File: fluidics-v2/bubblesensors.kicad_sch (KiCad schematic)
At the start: 6 parts, among them U8 TC7PZ17FU, U9 CD4050BDR

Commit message: started layout
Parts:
- renumbered C3 to C?, C4 to C?, U9 to U10, U8 to U11
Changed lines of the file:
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@@
   (symbol (lib_id "TC7PZ17FU:TC7PZ17FU") (at 41.91 22.86 0) (unit 1)
     (in_bom yes) (on_board yes) (dnp no)
-    (property "Reference" "U8" (at 40.64 20.32 0)
+    (property "Reference" "U11" (at 40.64 20.32 0)
       (effects (font (size 1.524 1.524)))
     )
@@
       (project "fluidics-v2"
         (path "/0ec91c42-8aad-437d-8c85-5e10f0e51fe0/f2389ff6-1cd8-47ea-9589-49f16bb8c559"
-          (reference "U8") (unit 1)
+          (reference "U11") (unit 1)
         )
       )
@@
   (symbol (lib_id "power:+3.3V") (at 29.21 64.77 0) (unit 1)
     (in_bom yes) (on_board yes) (dnp no)
-    (property "Reference" "#PWR061" (at 29.21 68.58 0)
+    (property "Reference" "#PWR?" (at 29.21 68.58 0)
       (effects (font (size 1.27 1.27)) hide)
     )
@@
       (project "fluidics-v2"
         (path "/0ec91c42-8aad-437d-8c85-5e10f0e51fe0/978ef52c-7a59-4000-92fc-4e58ca2b1aa7"
-          (reference "#PWR0131") (unit 1)
-        )
-        (path "/0ec91c42-8aad-437d-8c85-5e10f0e51fe0/f2389ff6-1cd8-47ea-9589-49f16bb8c559"
-          (reference "#PWR0128") (unit 1)
+          (reference "#PWR?") (unit 1)
+        )
+        (path "/0ec91c42-8aad-437d-8c85-5e10f0e51fe0/f2389ff6-1cd8-47ea-9589-49f16bb8c559"
+          (reference "#PWR0124") (unit 1)
         )
       )
@@
   (symbol (lib_id "Device:C") (at 29.21 68.58 0) (unit 1)
     (in_bom yes) (on_board yes) (dnp no)
-    (property "Reference" "C3" (at 25.4 71.12 0)
+    (property "Reference" "C?" (at 25.4 71.12 0)
       (effects (font (size 1.27 1.27)) (justify left))
     )
@@
       (project "fluidics-v2"
         (path "/0ec91c42-8aad-437d-8c85-5e10f0e51fe0/c1c30de3-a3db-48df-8d6b-b2f91b9251f0"
-          (reference "C3") (unit 1)
-        )
-        (path "/0ec91c42-8aad-437d-8c85-5e10f0e51fe0/978ef52c-7a59-4000-92fc-4e58ca2b1aa7"
-          (reference "C38") (unit 1)
-        )
-        (path "/0ec91c42-8aad-437d-8c85-5e10f0e51fe0/f2389ff6-1cd8-47ea-9589-49f16bb8c559"
-          (reference "C36") (unit 1)
+          (reference "C?") (unit 1)
+        )
+        (path "/0ec91c42-8aad-437d-8c85-5e10f0e51fe0/978ef52c-7a59-4000-92fc-4e58ca2b1aa7"
+          (reference "C?") (unit 1)
+        )
+        (path "/0ec91c42-8aad-437d-8c85-5e10f0e51fe0/f2389ff6-1cd8-47ea-9589-49f16bb8c559"
+          (reference "C21") (unit 1)
         )
       )
@@
   (symbol (lib_id "power:GND") (at 40.64 93.98 0) (unit 1)
     (in_bom yes) (on_board yes) (dnp no) (fields_autoplaced)
-    (property "Reference" "#PWR0131" (at 40.64 100.33 0)
+    (property "Reference" "#PWR0128" (at 40.64 100.33 0)
       (effects (font (size 1.27 1.27)) hide)
     )
@@
       (project "fluidics-v2"
         (path "/0ec91c42-8aad-437d-8c85-5e10f0e51fe0/f2389ff6-1cd8-47ea-9589-49f16bb8c559"
-          (reference "#PWR0131") (unit 1)
+          (reference "#PWR0128") (unit 1)
         )
       )
@@
   (symbol (lib_id "Device:C") (at 25.4 44.45 0) (unit 1)
     (in_bom yes) (on_board yes) (dnp no)
-    (property "Reference" "C4" (at 21.59 46.99 0)
+    (property "Reference" "C?" (at 21.59 46.99 0)
       (effects (font (size 1.27 1.27)) (justify left))
     )
@@
       (project "fluidics-v2"
         (path "/0ec91c42-8aad-437d-8c85-5e10f0e51fe0/c1c30de3-a3db-48df-8d6b-b2f91b9251f0"
-          (reference "C4") (unit 1)
-        )
-        (path "/0ec91c42-8aad-437d-8c85-5e10f0e51fe0/978ef52c-7a59-4000-92fc-4e58ca2b1aa7"
-          (reference "C37") (unit 1)
-        )
-        (path "/0ec91c42-8aad-437d-8c85-5e10f0e51fe0/f2389ff6-1cd8-47ea-9589-49f16bb8c559"
-          (reference "C33") (unit 1)
+          (reference "C?") (unit 1)
+        )
+        (path "/0ec91c42-8aad-437d-8c85-5e10f0e51fe0/978ef52c-7a59-4000-92fc-4e58ca2b1aa7"
+          (reference "C?") (unit 1)
+        )
+        (path "/0ec91c42-8aad-437d-8c85-5e10f0e51fe0/f2389ff6-1cd8-47ea-9589-49f16bb8c559"
+          (reference "C20") (unit 1)
         )
       )
@@
   (symbol (lib_id "power:GND") (at 35.56 48.26 0) (unit 1)
     (in_bom yes) (on_board yes) (dnp no)
-    (property "Reference" "#PWR0124" (at 35.56 54.61 0)
+    (property "Reference" "#PWR?" (at 35.56 54.61 0)
       (effects (font (size 1.27 1.27)) hide)
     )
@@
       (project "fluidics-v2"
         (path "/0ec91c42-8aad-437d-8c85-5e10f0e51fe0/978ef52c-7a59-4000-92fc-4e58ca2b1aa7"
-          (reference "#PWR0132") (unit 1)
+          (reference "#PWR?") (unit 1)
         )
         (path "/0ec91c42-8aad-437d-8c85-5e10f0e51fe0/f2389ff6-1cd8-47ea-9589-49f16bb8c559"
@@
   (symbol (lib_id "Device:C") (at 35.56 44.45 0) (unit 1)
     (in_bom yes) (on_board yes) (dnp no)
-    (property "Reference" "C3" (at 31.75 46.99 0)
+    (property "Reference" "C?" (at 31.75 46.99 0)
       (effects (font (size 1.27 1.27)) (justify left))
     )
@@
       (project "fluidics-v2"
         (path "/0ec91c42-8aad-437d-8c85-5e10f0e51fe0/c1c30de3-a3db-48df-8d6b-b2f91b9251f0"
-          (reference "C3") (unit 1)
-        )
-        (path "/0ec91c42-8aad-437d-8c85-5e10f0e51fe0/978ef52c-7a59-4000-92fc-4e58ca2b1aa7"
-          (reference "C38") (unit 1)
-        )
-        (path "/0ec91c42-8aad-437d-8c85-5e10f0e51fe0/f2389ff6-1cd8-47ea-9589-49f16bb8c559"
-          (reference "C34") (unit 1)
+          (reference "C?") (unit 1)
+        )
+        (path "/0ec91c42-8aad-437d-8c85-5e10f0e51fe0/978ef52c-7a59-4000-92fc-4e58ca2b1aa7"
+          (reference "C?") (unit 1)
+        )
+        (path "/0ec91c42-8aad-437d-8c85-5e10f0e51fe0/f2389ff6-1cd8-47ea-9589-49f16bb8c559"
+          (reference "C22") (unit 1)
         )
       )
@@
   (symbol (lib_id "Device:C") (at 19.05 68.58 0) (unit 1)
     (in_bom yes) (on_board yes) (dnp no)
-    (property "Reference" "C4" (at 15.24 71.12 0)
+    (property "Reference" "C?" (at 15.24 71.12 0)
       (effects (font (size 1.27 1.27)) (justify left))
     )
@@
       (project "fluidics-v2"
         (path "/0ec91c42-8aad-437d-8c85-5e10f0e51fe0/c1c30de3-a3db-48df-8d6b-b2f91b9251f0"
-          (reference "C4") (unit 1)
-        )
-        (path "/0ec91c42-8aad-437d-8c85-5e10f0e51fe0/978ef52c-7a59-4000-92fc-4e58ca2b1aa7"
-          (reference "C37") (unit 1)
-        )
-        (path "/0ec91c42-8aad-437d-8c85-5e10f0e51fe0/f2389ff6-1cd8-47ea-9589-49f16bb8c559"
-          (reference "C35") (unit 1)
+          (reference "C?") (unit 1)
+        )
+        (path "/0ec91c42-8aad-437d-8c85-5e10f0e51fe0/978ef52c-7a59-4000-92fc-4e58ca2b1aa7"
+          (reference "C?") (unit 1)
+        )
+        (path "/0ec91c42-8aad-437d-8c85-5e10f0e51fe0/f2389ff6-1cd8-47ea-9589-49f16bb8c559"
+          (reference "C19") (unit 1)
         )
       )
@@
   (symbol (lib_id "power:GND") (at 107.95 88.9 0) (unit 1)
     (in_bom yes) (on_board yes) (dnp no) (fields_autoplaced)
-    (property "Reference" "#PWR0130" (at 107.95 95.25 0)
+    (property "Reference" "#PWR0129" (at 107.95 95.25 0)
       (effects (font (size 1.27 1.27)) hide)
     )
@@
       (project "fluidics-v2"
         (path "/0ec91c42-8aad-437d-8c85-5e10f0e51fe0/f2389ff6-1cd8-47ea-9589-49f16bb8c559"
-          (reference "#PWR0130") (unit 1)
+          (reference "#PWR0129") (unit 1)
         )
       )
@@
   (symbol (lib_id "CD4050BDR:CD4050BDR") (at 40.64 76.2 0) (unit 1)
     (in_bom yes) (on_board yes) (dnp no) (fields_autoplaced)
-    (property "Reference" "U9" (at 68.58 66.04 0)
+    (property "Reference" "U10" (at 68.58 66.04 0)
       (effects (font (size 1.524 1.524)))
     )
@@
       (project "fluidics-v2"
         (path "/0ec91c42-8aad-437d-8c85-5e10f0e51fe0/f2389ff6-1cd8-47ea-9589-49f16bb8c559"
-          (reference "U9") (unit 1)
+          (reference "U10") (unit 1)
         )
       )
@@
   (symbol (lib_id "power:GND") (at 29.21 72.39 0) (unit 1)
     (in_bom yes) (on_board yes) (dnp no)
-    (property "Reference" "#PWR0124" (at 29.21 78.74 0)
+    (property "Reference" "#PWR?" (at 29.21 78.74 0)
       (effects (font (size 1.27 1.27)) hide)
     )
@@
       (project "fluidics-v2"
         (path "/0ec91c42-8aad-437d-8c85-5e10f0e51fe0/978ef52c-7a59-4000-92fc-4e58ca2b1aa7"
-          (reference "#PWR0132") (unit 1)
-        )
-        (path "/0ec91c42-8aad-437d-8c85-5e10f0e51fe0/f2389ff6-1cd8-47ea-9589-49f16bb8c559"
-          (reference "#PWR0129") (unit 1)
-        )
-      )
+          (reference "#PWR?") (unit 1)
+        )
+        (path "/0ec91c42-8aad-437d-8c85-5e10f0e51fe0/f2389ff6-1cd8-47ea-9589-49f16bb8c559"
+          (reference "#PWR0125") (unit 1)
+        )
+      )

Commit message: added pressure controllers and more flow sensors
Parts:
- C? (x2): footprint Capacitor_SMD:C_0603_1608Metric -> Capacitor_SMD:C_0805_2012Metric
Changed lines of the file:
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@@
       (effects (font (size 1.27 1.27)) (justify left))
     )
-    (property "Footprint" "Capacitor_SMD:C_0603_1608Metric" (at 30.1752 72.39 0)
+    (property "Footprint" "Capacitor_SMD:C_0805_2012Metric" (at 30.1752 72.39 0)
       (effects (font (size 1.27 1.27)) hide)
     )
@@
       (effects (font (size 1.27 1.27)) (justify left))
     )
-    (property "Footprint" "Capacitor_SMD:C_0603_1608Metric" (at 36.5252 48.26 0)
+    (property "Footprint" "Capacitor_SMD:C_0805_2012Metric" (at 36.5252 48.26 0)
       (effects (font (size 1.27 1.27)) hide)
     )

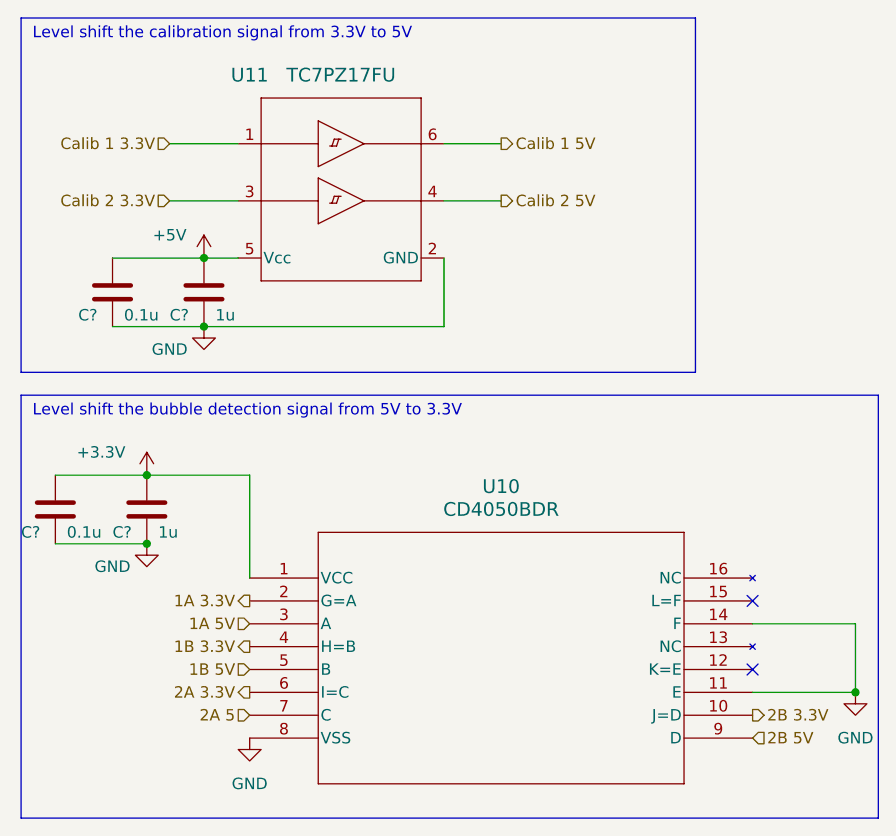
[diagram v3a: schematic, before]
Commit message: added new connector for motor control daughter board. began layout
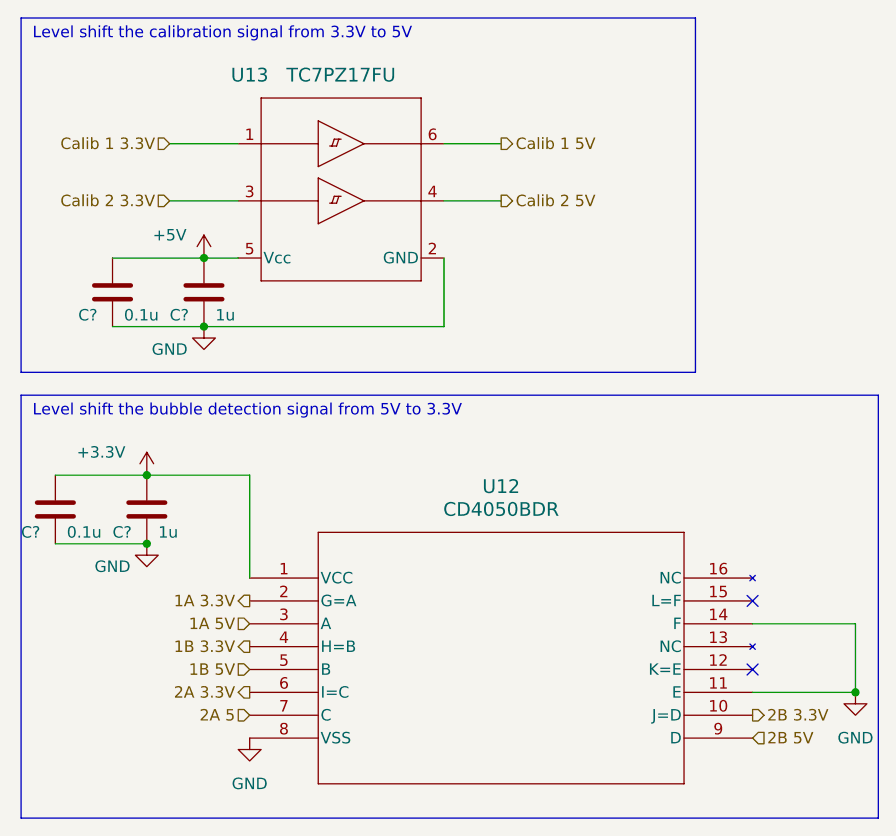
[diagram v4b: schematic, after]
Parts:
- renumbered U10 to U12, U11 to U13
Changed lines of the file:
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@@
   (symbol (lib_id "TC7PZ17FU:TC7PZ17FU") (at 41.91 22.86 0) (unit 1)
     (in_bom yes) (on_board yes) (dnp no)
-    (property "Reference" "U11" (at 40.64 20.32 0)
+    (property "Reference" "U13" (at 40.64 20.32 0)
       (effects (font (size 1.524 1.524)))
     )
@@
       (project "fluidics-v2"
         (path "/0ec91c42-8aad-437d-8c85-5e10f0e51fe0/f2389ff6-1cd8-47ea-9589-49f16bb8c559"
-          (reference "U11") (unit 1)
+          (reference "U13") (unit 1)
         )
       )
@@
         )
         (path "/0ec91c42-8aad-437d-8c85-5e10f0e51fe0/f2389ff6-1cd8-47ea-9589-49f16bb8c559"
-          (reference "#PWR0124") (unit 1)
+          (reference "#PWR0147") (unit 1)
         )
       )
@@
         )
         (path "/0ec91c42-8aad-437d-8c85-5e10f0e51fe0/f2389ff6-1cd8-47ea-9589-49f16bb8c559"
-          (reference "C21") (unit 1)
+          (reference "C23") (unit 1)
         )
       )
@@
   (symbol (lib_id "power:GND") (at 40.64 93.98 0) (unit 1)
     (in_bom yes) (on_board yes) (dnp no) (fields_autoplaced)
-    (property "Reference" "#PWR0128" (at 40.64 100.33 0)
+    (property "Reference" "#PWR0151" (at 40.64 100.33 0)
       (effects (font (size 1.27 1.27)) hide)
     )
@@
       (project "fluidics-v2"
         (path "/0ec91c42-8aad-437d-8c85-5e10f0e51fe0/f2389ff6-1cd8-47ea-9589-49f16bb8c559"
-          (reference "#PWR0128") (unit 1)
+          (reference "#PWR0151") (unit 1)
         )
       )
@@
         )
         (path "/0ec91c42-8aad-437d-8c85-5e10f0e51fe0/f2389ff6-1cd8-47ea-9589-49f16bb8c559"
-          (reference "C20") (unit 1)
+          (reference "C22") (unit 1)
         )
       )
@@
         )
         (path "/0ec91c42-8aad-437d-8c85-5e10f0e51fe0/f2389ff6-1cd8-47ea-9589-49f16bb8c559"
-          (reference "#PWR0127") (unit 1)
+          (reference "#PWR0150") (unit 1)
         )
       )
@@
   (symbol (lib_id "power:+5V") (at 35.56 40.64 0) (unit 1)
     (in_bom yes) (on_board yes) (dnp no)
-    (property "Reference" "#PWR0126" (at 35.56 44.45 0)
+    (property "Reference" "#PWR0149" (at 35.56 44.45 0)
       (effects (font (size 1.27 1.27)) hide)
     )
@@
       (project "fluidics-v2"
         (path "/0ec91c42-8aad-437d-8c85-5e10f0e51fe0/f2389ff6-1cd8-47ea-9589-49f16bb8c559"
-          (reference "#PWR0126") (unit 1)
+          (reference "#PWR0149") (unit 1)
         )
       )
@@
         )
         (path "/0ec91c42-8aad-437d-8c85-5e10f0e51fe0/f2389ff6-1cd8-47ea-9589-49f16bb8c559"
-          (reference "C22") (unit 1)
+          (reference "C24") (unit 1)
         )
       )
@@
         )
         (path "/0ec91c42-8aad-437d-8c85-5e10f0e51fe0/f2389ff6-1cd8-47ea-9589-49f16bb8c559"
-          (reference "C19") (unit 1)
+          (reference "C21") (unit 1)
         )
       )
@@
   (symbol (lib_id "power:GND") (at 107.95 88.9 0) (unit 1)
     (in_bom yes) (on_board yes) (dnp no) (fields_autoplaced)
-    (property "Reference" "#PWR0129" (at 107.95 95.25 0)
+    (property "Reference" "#PWR0152" (at 107.95 95.25 0)
       (effects (font (size 1.27 1.27)) hide)
     )
@@
       (project "fluidics-v2"
         (path "/0ec91c42-8aad-437d-8c85-5e10f0e51fe0/f2389ff6-1cd8-47ea-9589-49f16bb8c559"
-          (reference "#PWR0129") (unit 1)
+          (reference "#PWR0152") (unit 1)
         )
       )
@@
   (symbol (lib_id "CD4050BDR:CD4050BDR") (at 40.64 76.2 0) (unit 1)
     (in_bom yes) (on_board yes) (dnp no) (fields_autoplaced)
-    (property "Reference" "U10" (at 68.58 66.04 0)
+    (property "Reference" "U12" (at 68.58 66.04 0)
       (effects (font (size 1.524 1.524)))
     )
@@
       (project "fluidics-v2"
         (path "/0ec91c42-8aad-437d-8c85-5e10f0e51fe0/f2389ff6-1cd8-47ea-9589-49f16bb8c559"
-          (reference "U10") (unit 1)
+          (reference "U12") (unit 1)
         )
       )
@@
         )
         (path "/0ec91c42-8aad-437d-8c85-5e10f0e51fe0/f2389ff6-1cd8-47ea-9589-49f16bb8c559"
-          (reference "#PWR0125") (unit 1)
-        )
-      )
+          (reference "#PWR0148") (unit 1)
+        )
+      )
